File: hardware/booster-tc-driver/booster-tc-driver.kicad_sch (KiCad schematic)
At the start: 110 parts, among them IC1 AD5160BRJZ5-RL7, IC2 AD5160BRJZ5-RL7, IC3 BD50FD0WHFP-TR, IC4 CAT4109V-GT2, IC5 L4940D2T12-TR, J1 62201021121, J10 3-647166-2, J2 EHT-105-01-S-D, J3 3-647166-2, J6 22-23-2021, J7 3-647166-2, J8 B4B-PH-SM4-TB, Q1 T2N7002AK, SW1 SW_SPDT, U1 STM32G474CBTx, U10 LT1963AxST-3.3, U2 AOZ1284PI, U3 CSTNE8M00G550000R0, U4 IF-D95T << must be T, U5 IF-E96E, U6 IF-D95T << must be T, U7 AOZ1284PI

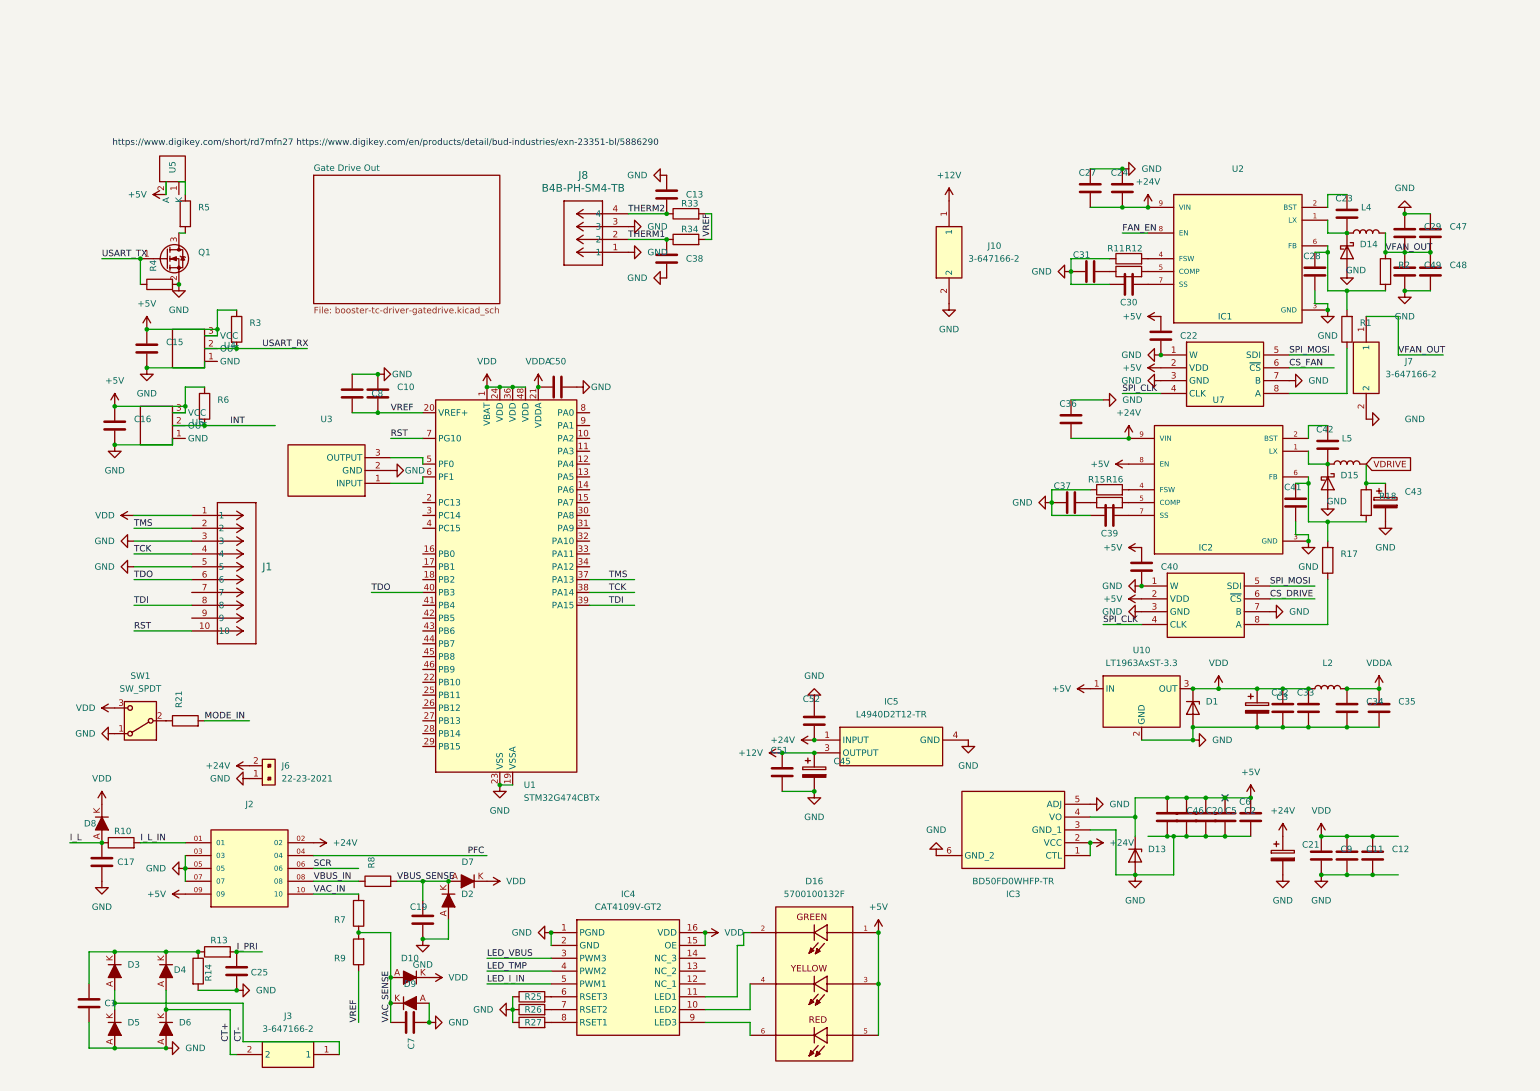
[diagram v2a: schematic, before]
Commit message: driver board+code
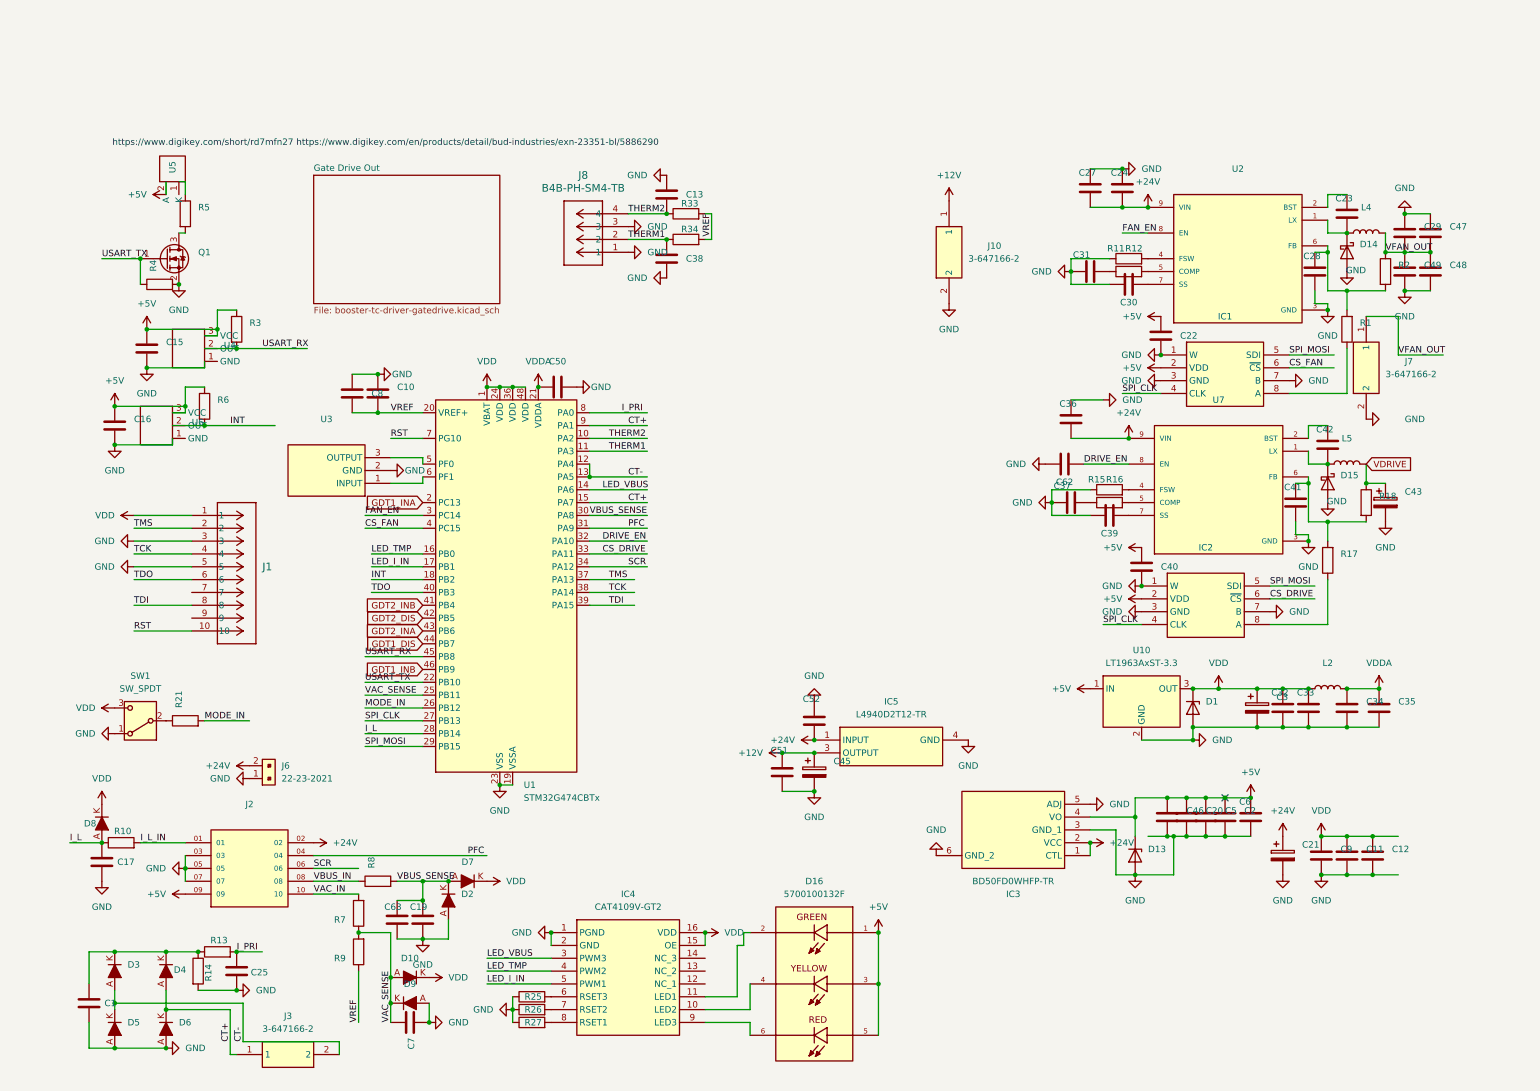
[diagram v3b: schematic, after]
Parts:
- added C62: 22n VJ0805Y223KBBBE31, Capacitor_SMD:C_0805_2012Metric_Pad1.18x1.45mm_HandSolder, symbol Device:C
- added C63: 10n VJ0603Y103KXJAC31X, Capacitor_SMD:C_0603_1608Metric_Pad1.08x0.95mm_HandSolder, symbol Device:C
- C7: value 1n CGA3EAC0G2A102J080AA -> 10n VJ0603Y103KXJAC31X
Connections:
- net +5V: no longer U7.8 (EN)
- net CS_DRIVE: now also U1.33 (PA11)
- net CS_FAN: now also U1.4 (PC15)
- net CT+: now also J3.1, U1.15 (PA7), U1.9 (PA1); no longer J3.2
- net CT-: now also J3.2, U1.12 (PA4), U1.13 (PA5); no longer J3.1
- net FAN_EN: now also U1.3 (PC14)
- net GND: now also C62.2, C63.2
- net INT: now also U1.18 (PB2)
- net I_L: now also U1.28 (PB14)
- net I_PRI: now also U1.8 (PA0)
- net LED_I_IN: now also U1.17 (PB1)
- net LED_TMP: now also U1.16 (PB0)
- net LED_VBUS: now also U1.14 (PA6)
- net MODE_IN: now also U1.26 (PB12)
- net PFC: now also U1.31 (PA9)
- net SCR: now also U1.34 (PA12)
- net SPI_CLK: now also U1.27 (PB13)
- net SPI_MOSI: now also U1.29 (PB15)
- net THERM1: now also U1.11 (PA3)
- net THERM2: now also U1.10 (PA2)
- net USART_RX: now also U1.45 (PB8)
- net USART_TX: now also U1.22 (PB10)
- net VAC_SENSE: now also U1.25 (PB11)
- net VBUS_SENSE: now also U1.30 (PA8), C63.1
- net GDT1_INA: now reaches U1.2 (PC13)
- net DRIVE_EN: now reaches U1.32 (PA10)
- net DRIVE_EN: now also U7.8 (EN), C62.1
- net GDT2_INB: now reaches U1.41 (PB4)
- net GDT2_DIS: now reaches U1.42 (PB5)
- net GDT2_INA: now reaches U1.43 (PB6)
- net GDT1_DIS: now reaches U1.44 (PB7)
- net GDT1_INB: now reaches U1.46 (PB9)
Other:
- moved on the sheet: J3

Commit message: driver board work
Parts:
- added C64, C65, C66, C71, C73, C74, C90, C91, C92, C93, C94, C95: .1uf 885012208087, Capacitor_SMD:C_1206_3216Metric_Pad1.33x1.80mm_HandSolder, symbol Device:C
- added C67, C68, C69, C70, C72, C75, C76, C77, C78, C79, C83, C84, C85, C86, C87, C88, C89: 2u2 C3225X7R1H225K250AB, Capacitor_SMD:C_1210_3225Metric_Pad1.33x2.70mm_HandSolder, symbol Device:C
- added C80, C81, C82: .1uf C0603C104K3RECTU, Capacitor_SMD:C_0603_1608Metric_Pad1.08x0.95mm_HandSolder, symbol Device:C
- C35: value .1uf 885012208087 -> .1uf C0603C104K3RECTU; footprint Capacitor_SMD:C_1206_3216Metric_Pad1.33x1.80mm_HandSolder -> Capacitor_SMD:C_0603_1608Metric_Pad1.08x0.95mm_HandSolder
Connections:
- net +12V: now also C64.1, C65.1, C66.1, C67.1, C68.1, C69.1, C70.1
- net +24V: now also C71.1, C74.1, C75.1, C76.1, C77.1, C78.1, C83.1, C84.1
- net +5V: now also C89.1
- net GND: now also C35.1, C64.2, C65.2, C66.2, C67.2, C68.2, C69.2, C70.2, C71.2, C72.2, C73.2, C74.2, C75.2, C76.2, C77.2, C78.2, C79.2, C80.1, C81.1, C82.1, C83.2, C84.2, C85.2, C86.2, C87.2, C88.2, C89.2, C90.2, C91.2, C92.2, C93.2, C94.2, C95.2; no longer C35.2
- net VDD: now also C85.1, C86.1, C87.1, C88.1, C90.1, C91.1, C92.1, C93.1, C94.1, C95.1
- net VDDA: now also C35.2; no longer C35.1
- net VDRIVE: now also C72.1, C73.1
- net VFAN_OUT: now also C79.1, C80.2, C81.2, C82.2
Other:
- moved on the sheet: C11, C12, C6, C9

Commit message: silkscreen + software cleanup
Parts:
- C3, C43, C45: value 330u 860020575013 -> 470u 860020474014; footprint Library:860020575013 -> Library:CAPPRD350W52D800H1300
- C72: value 2u2 C3225X7R1H225K250AB -> .1uf 885012208087; footprint Capacitor_SMD:C_1210_3225Metric_Pad1.33x2.70mm_HandSolder -> Capacitor_SMD:C_1206_3216Metric_Pad1.33x1.80mm_HandSolder
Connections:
- net INT: now also U1.34 (PA12); no longer U1.18 (PB2)
- net SCR: now also U1.18 (PB2); no longer U1.34 (PA12)
- net VDD: no longer C85.1
- net VDRIVE: now also C85.1

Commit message: schematic cleanup
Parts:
- L4, L5: value 22u 7443551221 -> 22u SRP7028A-220M; footprint Library:7443551221 -> Library:INDPM7366X300N
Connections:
- net I_L_IN: no longer names the net of J2.01, R10.2
- net VAC_IN: no longer names the net of J2.10, R7.2
- net VBUS_IN: no longer names the net of J2.08, R8.1
- no-connect marks 1 -> 0
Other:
- moved on the sheet: C11, C12, C15, C16, C21, C7, C71, C74, C75, C76, C77, C78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

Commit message: changed pin assignments, improved hardware
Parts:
- removed C65, C90, C91, C92, C93, C94, C95: .1uf 885012208087, Capacitor_SMD:C_1206_3216Metric_Pad1.33x1.80mm_HandSolder, symbol Device:C
- removed C67, C68, C69, C70, C75, C76, C77, C78, C83, C84, C86, C87, C88: 2u2 C3225X7R1H225K250AB, Capacitor_SMD:C_1210_3225Metric_Pad1.33x2.70mm_HandSolder, symbol Device:C
- removed IC5: L4940D2T12-TR, Library:L4940D2T12-TR, symbol New_Library:L4940D2T12-TR
- added C96: .1uf 885012208087, Capacitor_SMD:C_1206_3216Metric_Pad1.33x1.80mm_HandSolder, symbol Device:C
- added D19: MBR0530, digikey-footprints:SOD-123, symbol dk_Diodes-Rectifiers-Single:1N5819HW-7-F
- added D20: PMEG4050EP, Diode_SMD:D_SOD-128, symbol Diode:PMEG4050EP
- added L1: 22u SRP7028A-220M, Library:INDPM7366X300N, symbol Device:L
- added Q2: NTR5198NLT1G, Library:SOT96P237X111-3N, symbol New_Library:NTR5198NLT1G
- added R19: 1k MCU0805MD1051BP500, Resistor_SMD:R_0805_2012Metric_Pad1.20x1.40mm_HandSolder, symbol Device:R
- added R20: 9k CRCW08059K10FKEAHP, Resistor_SMD:R_0805_2012Metric_Pad1.20x1.40mm_HandSolder, symbol Device:R
- added R35: 10k CRCW080510K0DHEAP, Resistor_SMD:R_0805_2012Metric_Pad1.20x1.40mm_HandSolder, symbol Device:R
- added R36: 150R KTR18EZPJ151, Resistor_SMD:R_1206_3216Metric_Pad1.30x1.75mm_HandSolder, symbol Device:R
- added U11: AP1501A-12K5G-13, Package_TO_SOT_SMD:TO-263-5_TabPin3, symbol New_Library:AP1501A-12K5G-13
- C29: value 2u2 C3225X7R1H225K250AB -> 1n CGA3EAC0G2A102J080AA; footprint Capacitor_SMD:C_1210_3225Metric_Pad1.33x2.70mm_HandSolder -> Capacitor_SMD:C_0603_1608Metric_Pad1.08x0.95mm_HandSolder
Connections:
- net GDT2_INA is gone; now on net GDT2_DIS: U1.43 (PB6)
- net +12V: now also L1.2, U11.4 (FB)
- net +24V: now also R20.1, U11.1 (VIN)
- net CT+: no longer U1.15 (PA7)
- net CT-: no longer U1.13 (PA5)
- net GDT2_DIS: no longer U1.42 (PB5)
- net GND: now also C29.2, J1.9, C96.2, D20.2 (A), Q2.2 (S), R19.1, R35.2, U11.3 (GND), U11.5 (SD); no longer C29.1, J10.2
- net INT: now also U1.13 (PA5); no longer U1.34 (PA12)
- net LED_I_IN: now also U1.16 (PB0); no longer U1.17 (PB1)
- net LED_TMP: now also U1.15 (PA7); no longer U1.16 (PB0)
- net VDD: now also D19.K
- net VFAN_OUT: no longer C29.2
- net VBUS_IN: now reaches J2.08, R8.1
- net I_L_IN: now reaches J2.01, R10.2
- net VAC_IN: now reaches J2.10, R7.2
- net GDT1_INA renamed PMP_EN
- net PMP_EN: now also R36.1
- net GDT1_INB renamed GDT_A
- net GDT2_INB: no longer names the net of U1.41 (PB4)
- new net: D20.1 (K), L1.1, U11.2 (VOUT)
- new net: C29.1, Q2.1 (G), R35.1, R36.2
- new net: J10.2, Q2.3 (D)
- new net 24V_SENSE: C96.1, D19.A, R19.2, R20.2, U1.17 (PB1)
- new net GDT_B: U1.42 (PB5)
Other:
- moved on the sheet: C45, C51, C52, C64, C66, J10

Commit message: ftdi board + random stuff
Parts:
- removed C85, C89: 2u2 C3225X7R1H225K250AB, Capacitor_SMD:C_1210_3225Metric_Pad1.33x2.70mm_HandSolder, symbol Device:C
- removed IC3: BD50FD0WHFP-TR, Library:BD50FD0WHFPTR, symbol New_Library:BD50FD0WHFP-TR
- removed J8: B4B-PH-SM4-TB, Library:CONN_B4B-PH-SM4-TB_JST, symbol New_Library:B4B-PH-SM4-TB
- added C65, C67: 150p VJ0603A151JXAAC, Capacitor_SMD:C_0603_1608Metric_Pad1.08x0.95mm_HandSolder, symbol Device:C
- added C68, C69: 10n VJ0603Y103KXJAC31X, Capacitor_SMD:C_0603_1608Metric_Pad1.08x0.95mm_HandSolder, symbol Device:C
- added C70: .1uf 885012208087, Capacitor_SMD:C_1206_3216Metric_Pad1.33x1.80mm_HandSolder, symbol Device:C
- added D21: MBR0530, digikey-footprints:SOD-123, symbol dk_Diodes-Rectifiers-Single:1N5819HW-7-F
- added IC3: LDL1117S50R, SOT230P700X180-4N, symbol New_Library:LDL1117S50R
- added J8, J9: 3-647166-2, Library:36471662, symbol New_Library:3-647166-2
- added R37: 1k, Resistor_SMD:R_0805_2012Metric_Pad1.20x1.40mm_HandSolder, symbol Device:R
- added U12: MCP9700Ax-ETT, Package_TO_SOT_SMD:SOT-23, symbol Sensor_Temperature:MCP9700Ax-ETT
- R1, R17: value 3k CRCW08053K00FKTA -> 3k
- R10, R13, R19, R21, R3, R4, R6, R7, R8, R9: value 1k MCU0805MD1051BP500 -> 1k
- R11, R15: value 47k CRCW080547K0FKEA -> 47k
- R12, R16: value 470k CRCW0805470KFKTA -> 470k
- R14: value 5R1 ERJ-B1BF5R1U -> 2R2 35222R2JT; footprint Resistor_SMD:R_1020_2550Metric_Pad1.33x5.20mm_HandSolder -> Resistor_SMD:R_2512_6332Metric_Pad1.40x3.35mm_HandSolder
- R18, R2: value 82k CRCW080582K0FKEA -> 82k
- R20: value 9k CRCW08059K10FKEAHP -> 9k
- R33, R34, R35: value 10k CRCW080510K0DHEAP -> 10k
- R36, R5: value 150R KTR18EZPJ151 -> 150R; footprint Resistor_SMD:R_1206_3216Metric_Pad1.30x1.75mm_HandSolder -> Resistor_SMD:R_0805_2012Metric_Pad1.20x1.40mm_HandSolder
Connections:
- net +12V: now also IC3.3 (VIN)
- net +5V: now also IC3.2 (VOUT_1), IC3.4 (VOUT_2)
- net CT+: now also C65.1
- net CT-: now also C67.1
- net GND: now also C65.2, C67.2, C68.2, C69.2, C70.1, IC3.1 (GND), J8.1, J9.1, U12.3 (GND)
- net I_PRI: now also D21.A
- net MODE_IN: now also U1.34 (PA12), C68.1; no longer U1.26 (PB12)
- net THERM1: now also J9.2
- net THERM2: now also J8.2
- net VDD: now also C70.2, D21.K, U12.1 (V_{DD})
- net JRST: now reaches U1.41 (PB4)
- new net: R37.1, U12.2 (V_{OUT})
- new net THERM_BOARD: C69.1, R37.2, U1.26 (PB12)
